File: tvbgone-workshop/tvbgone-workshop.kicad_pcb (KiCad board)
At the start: 2 copper layers, 64.1 x 54.6 mm, 25 parts, among them CON1 AVR-ISP-6, IC1 ATTINY85-S, Q1 MOSFET_N, Q2 MOSFET_N, SW1 SW_PUSH_SMALL, X1 8MHz

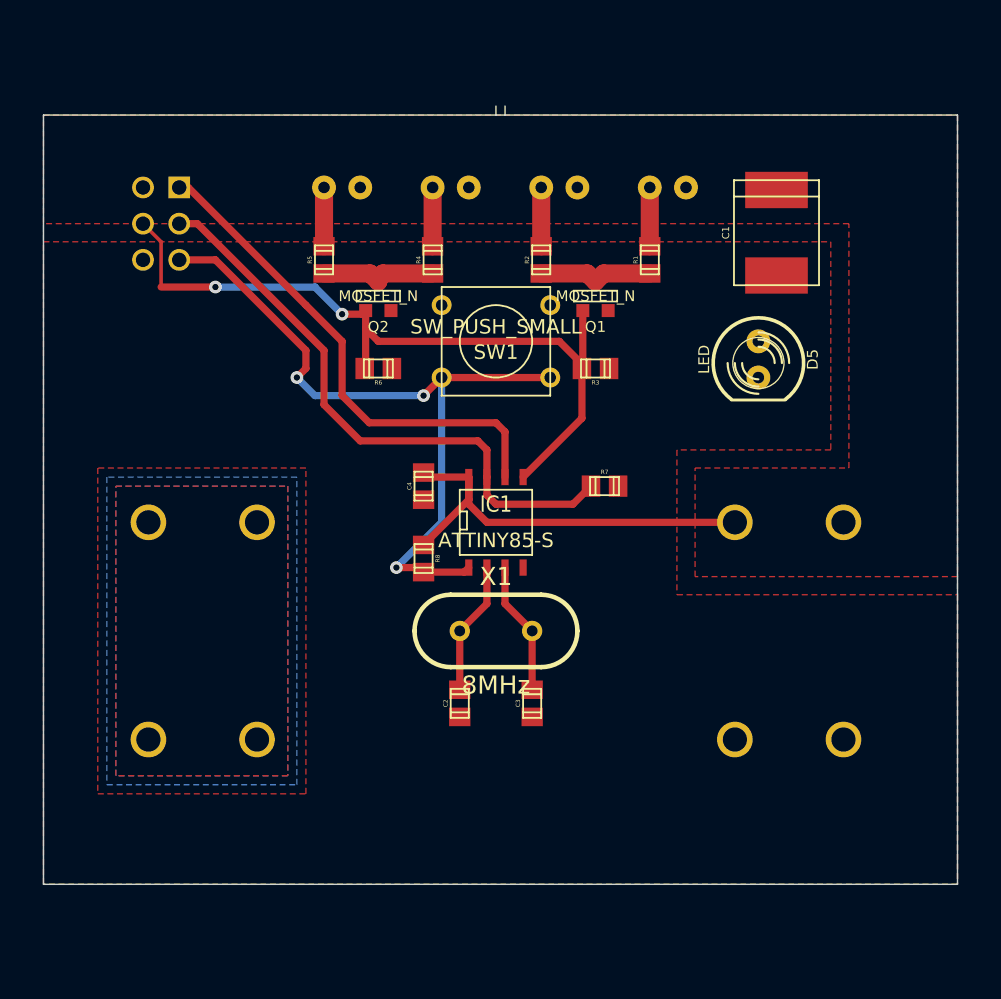
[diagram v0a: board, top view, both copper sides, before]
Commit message: add holes, changes size of the board a bit, shuffle stuf around
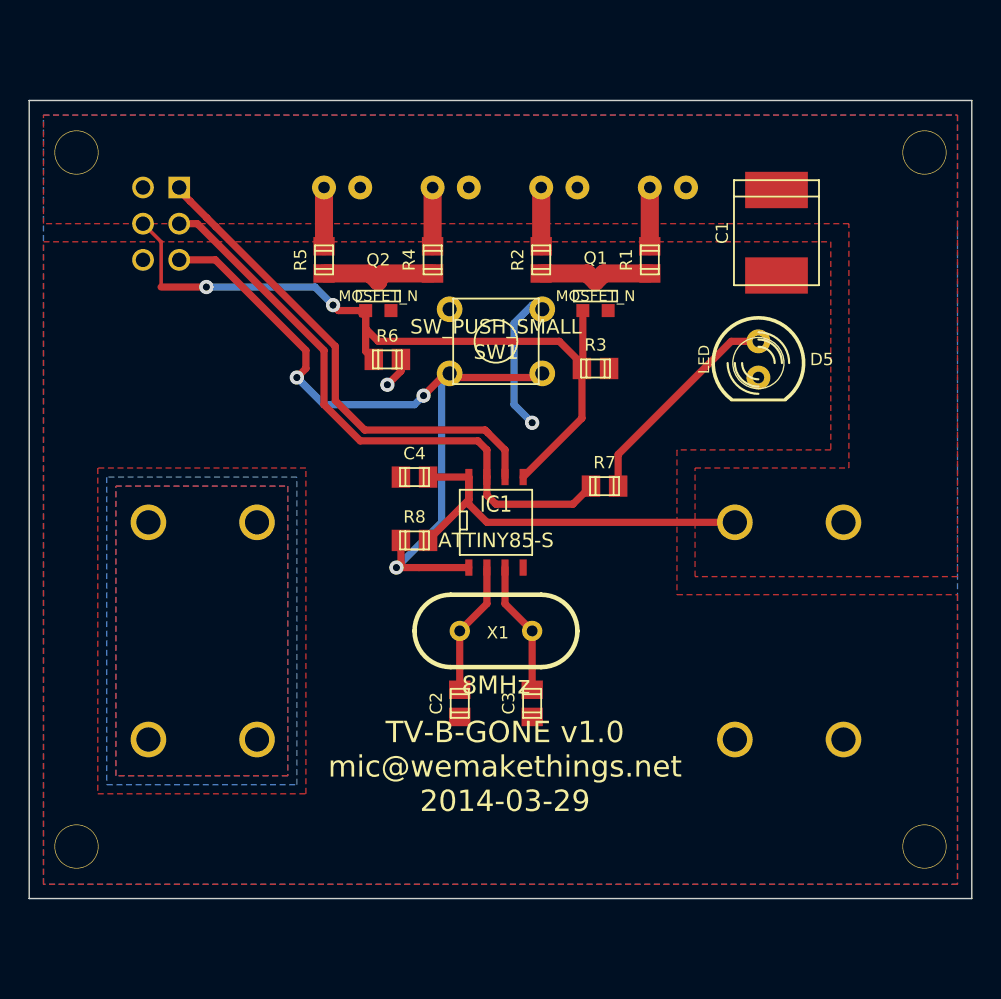
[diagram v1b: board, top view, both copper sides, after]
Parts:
- added ?: VAL**, MECH-HOLE220, F.Cu at (87.6, 124.6)
- added MECH-HOLE220: VAL**, MECH-HOLE220, F.Cu at (146.2, 124.0)
- added MECH-HOLE220: VAL**, MECH-HOLE220, F.Cu at (88.3, 76.3)
- added MECH-HOLE220: VAL**, MECH-HOLE220, F.Cu at (146.2, 75.9)
- moved R8 1.42 mm to (111.1, 102.9), turned to 180 degrees
- moved C4 0.90 mm to (111.1, 98.4), turned to 0 degrees
- moved R6 0.90 mm to (109.2, 90.2)
- renumbered CON1 to ISP
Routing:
- net N-000008: track 0.00 -> 15.4 mm
- net GND: track 0.00 -> 12.7 mm, vias 0 -> 2
- net /RESET: track 52.5 -> 54.8 mm
- net /MOSI: track 54.2 -> 55.2 mm
- net /MISO: track 35.4 -> 34.7 mm
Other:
- board size 64.1 x 54.6 mm -> 66.1 x 56 mm
- net class Default: via_dia 0.889 -> 1; via_drill 0.635 -> 0.5
- rule via_min_drill: 0.508 -> 0.5
- rule via_min_size: 0.889 -> 1
- board text added: "TV-B-GONE v1.0 mic@wemakethings.net 2014-03-29"

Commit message: opit
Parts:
- added >VALUE: >NAME, dallas-SOIC-8, F.Cu at (128.5, 127.0)
- moved BT1 1.14 mm to (117.2, 100.5)
- moved BT2 0.73 mm to (117.2, 117.5)
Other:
- board size 66.1 x 56 mm -> 56.1 x 66 mm

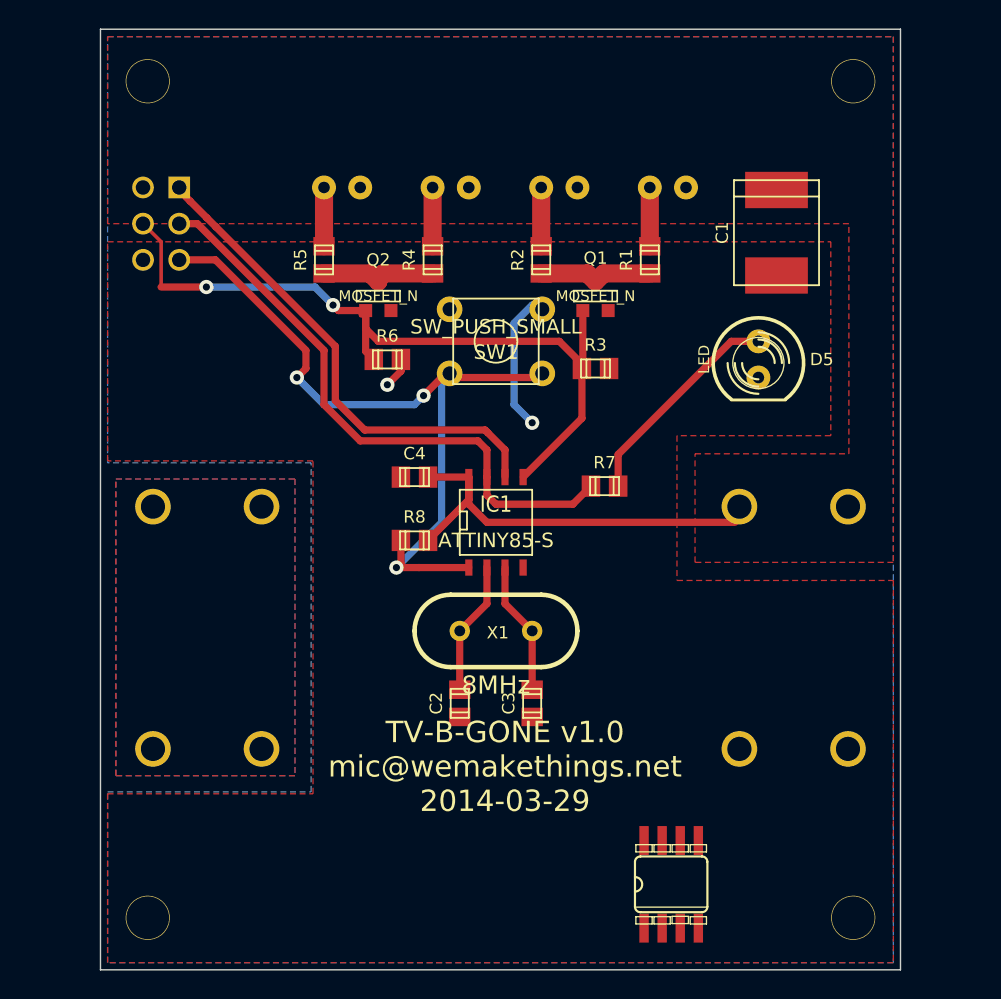
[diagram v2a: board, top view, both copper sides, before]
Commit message: changed MCU package, a bit more silkscreen markings for batteries and a polar cap
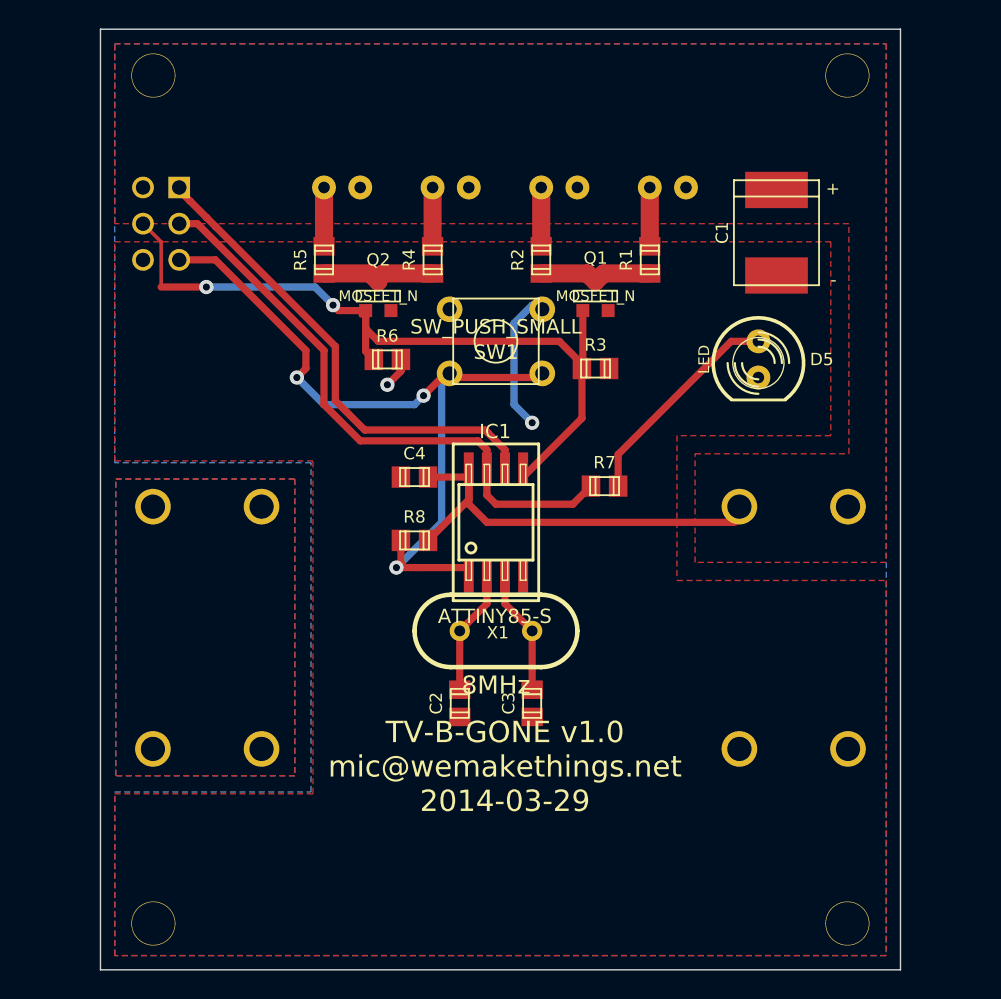
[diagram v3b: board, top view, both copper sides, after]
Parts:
- removed >VALUE: >NAME, dallas-SOIC-8
- removed MECH-HOLE220: VAL**, MECH-HOLE220
- added ?: VAL**, MECH-HOLE220, F.Cu at (88.3, 76.3)
- BT2: footprint BATT-AA-BK92 -> BATT-AA-BK92-bold
- IC1: footprint SO8N -> SO8_200mil_wide
- renumbered MECH-HOLE220 to ?

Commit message: move to the new kicad, play around with 3d packages, make pads bigger for easier soldering
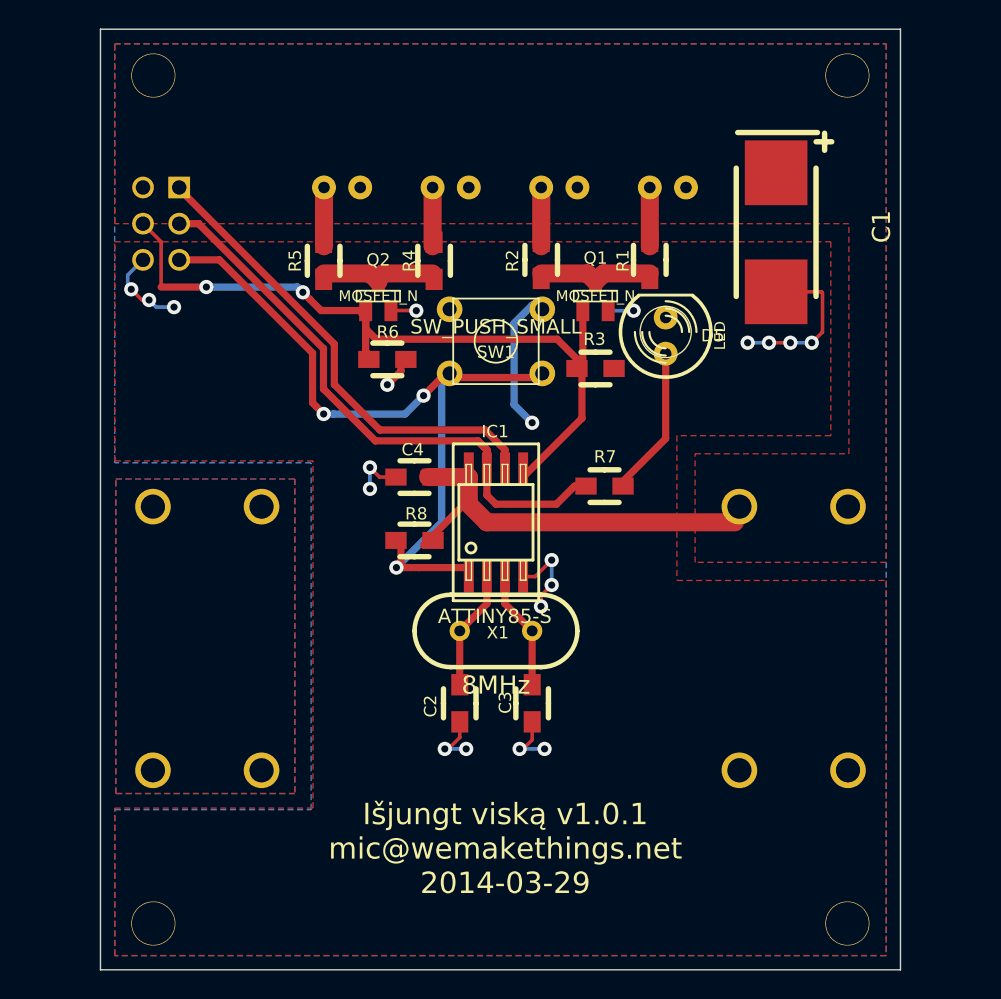
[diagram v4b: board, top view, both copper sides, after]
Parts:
- C1: footprint c_tant_E -> Capacitors_Tantalum_SMD:TantalC_SizeE_EIA-7360_HandSoldering
- C2, C3, C4, R1, R2, R3, R4, R5, R6, R7, R8: footprint c_0805 -> Resistors_SMD:Resistor_SMD0805_HandSoldering
- moved D5 6.72 mm to (128.8, 88.5), turned to 90 degrees
- moved BT2 1.50 mm to (117.2, 119.0)
- moved R4 0.12 mm to (112.5, 83.2), turned to 270 degrees
- moved R5 0.07 mm to (104.8, 83.2), turned to 270 degrees
- turned C1 to 270 degrees
- turned C2 to 270 degrees
- turned C3 to 270 degrees
- turned C4 to 180 degrees
- turned R1 to 270 degrees
- turned R2 to 270 degrees
- turned R3 to 0 degrees
- turned R6 to 0 degrees
- turned R7 to 180 degrees
- turned R8 to 0 degrees
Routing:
- net GND: track 12.7 -> 51.8 mm, vias 2 -> 20
- net N-000008: track 15.4 -> 10.7 mm
- net /SCK: track 41.7 -> 43.3 mm
- net /MISO: track 34.7 -> 34.1 mm
- net /RESET: track 54.8 -> 55.4 mm
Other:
- board text added: "Išjungt viską v1.0.1 mic@wemakethings.net 2014-03-29"
- board text removed: "TV-B-GONE v1.0 mic@wemakethings.net 2014-03-29"

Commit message: some leftovers
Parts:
- added SYM: Symbol_OSHW-Logo_SilkScreen_07Jul2012, Symbols:Symbol_OSHW-Logo_SilkScreen, B.Cu at (137.2, 77.5)
- moved C1 0.61 mm to (135.9, 81.3)
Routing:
- net GND: track 51.8 -> 50.0 mm, vias 20 -> 19
- net (no net): track 0.00 -> 1.75 mm, vias 0 -> 1
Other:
- board text added: "Išjungt viską v1.0.1 mic@wemakethings.net 2014-10-13"
- board text added: "TECHNARIUMAS.LT WEMAKETHINGS.NET"
- board text removed: "Išjungt viską v1.0.1 mic@wemakethings.net 2014-03-29"
